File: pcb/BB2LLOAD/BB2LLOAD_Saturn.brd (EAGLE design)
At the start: 53.2 x 53.2 mm, 2 parts, among them K1 685119134923

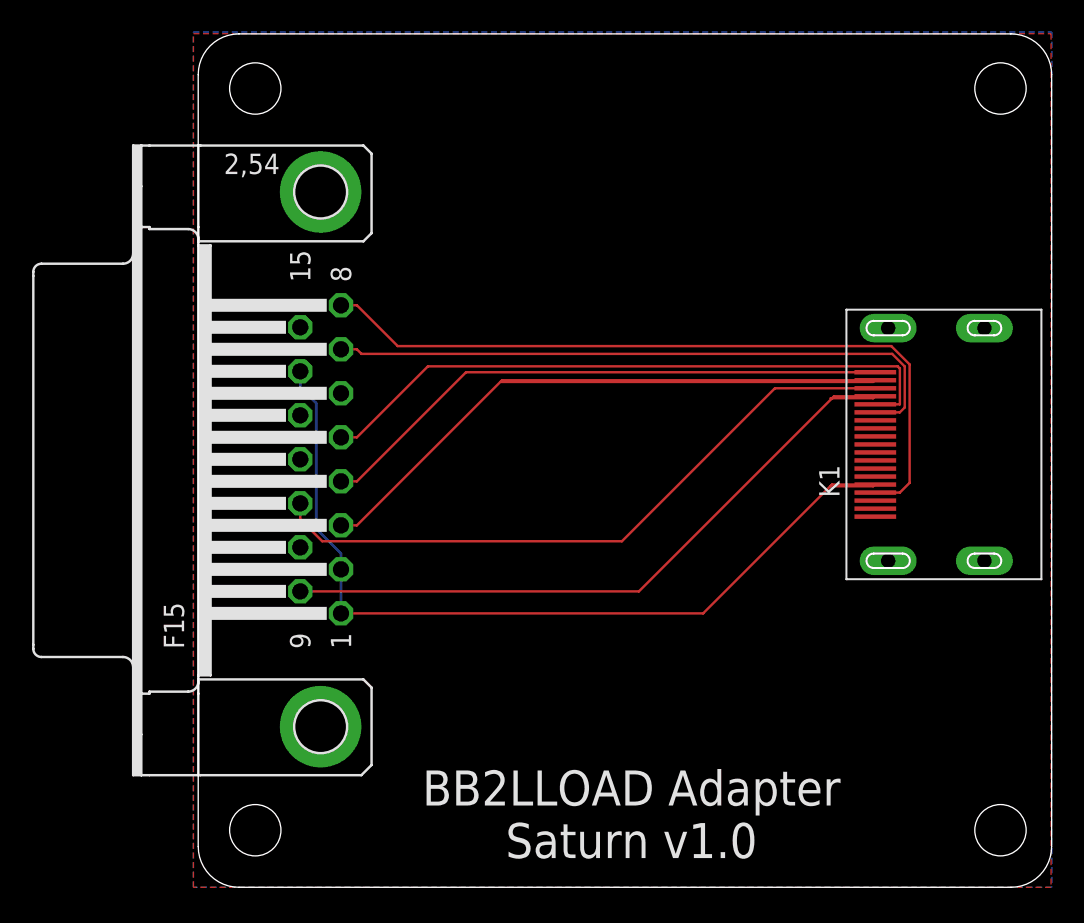
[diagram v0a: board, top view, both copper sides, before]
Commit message: Changed form factor of the bb2load pcb (slim)
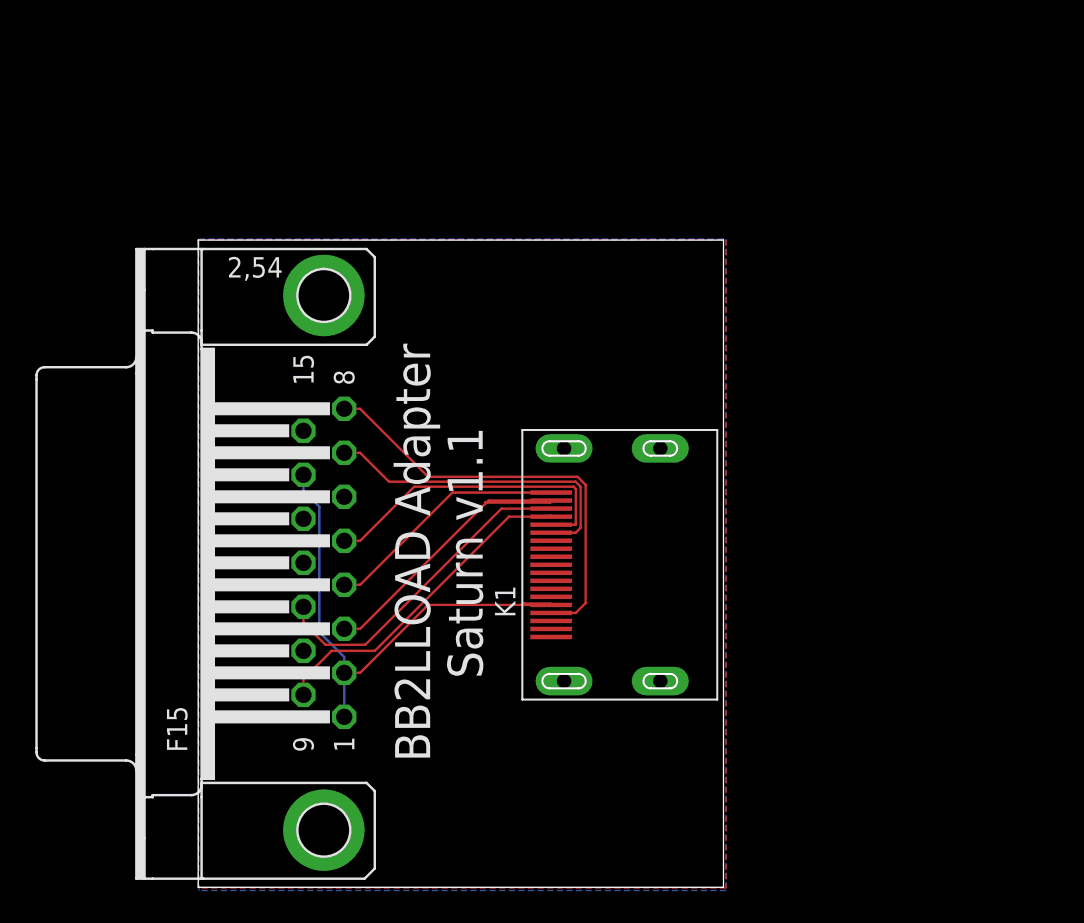
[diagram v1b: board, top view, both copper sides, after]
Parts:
- moved K1 21.5 mm to (22.0, 20.1)
- moved X3 6.45 mm to (7.83, 20.2)
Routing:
- net P3: track 60.4 -> 20.5 mm
- net P9: track 43.8 -> 20.8 mm
- net GND: track 55.6 -> 32.7 mm
- net P4: track 36.2 -> 15.4 mm
- net P11: track 41.5 -> 20.6 mm
- net P5: track 40.5 -> 19.6 mm
- net P7: track 40.1 -> 20.1 mm
- net VCC: track 46.8 -> 26.9 mm
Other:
- board size 53.2 x 53.2 mm -> 32.7 x 40.3 mm
- board text added: "BB2LLOAD Adapter Saturn v1.1"
- board text removed: "BB2LLOAD Adapter Saturn v1.0"
